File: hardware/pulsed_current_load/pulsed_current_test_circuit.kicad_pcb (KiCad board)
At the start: 2 copper layers, 50 x 50 mm, 19 parts, among them J1 Conn_02x03_Odd_Even, J2 Conn_02x03_Odd_Even, U1 eALD1116SAL, U2 eALD1116SAL, U3 eALD1116SAL

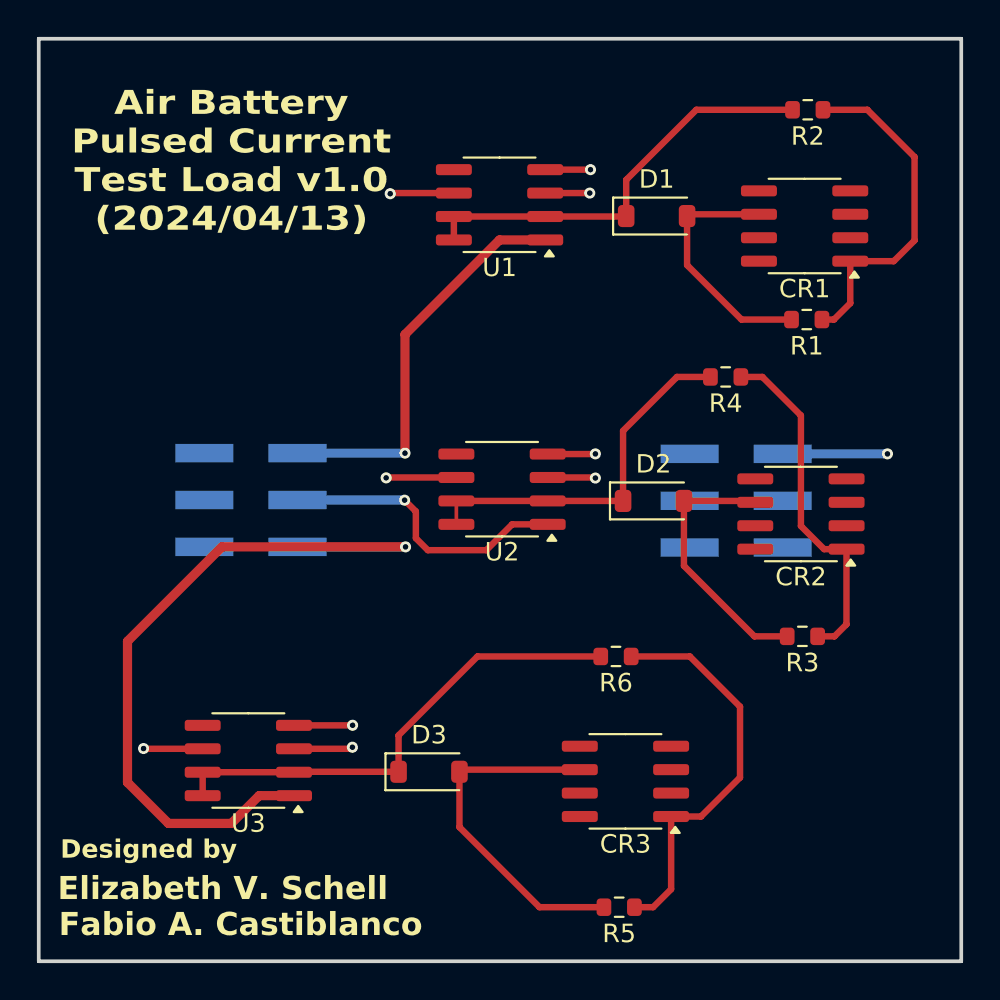
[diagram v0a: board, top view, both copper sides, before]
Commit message: added resistor load test board and adjustments to pulsed current load
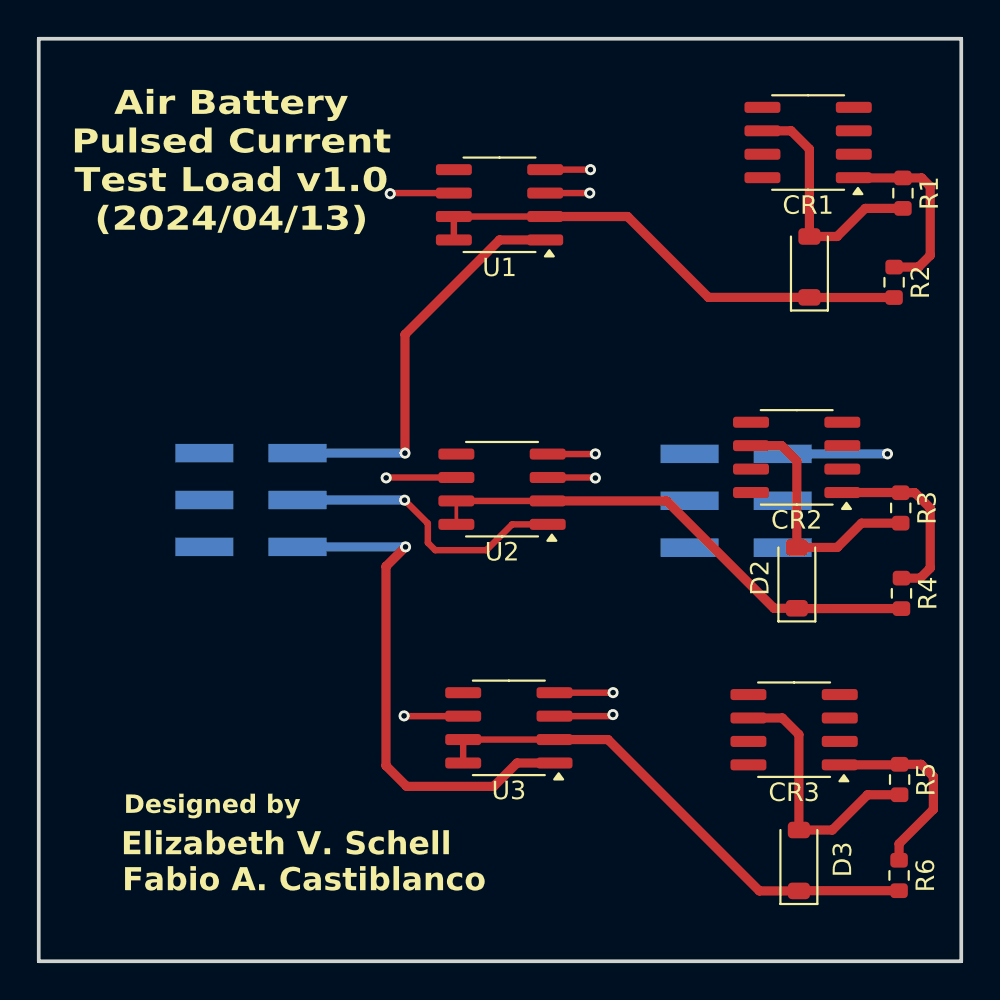
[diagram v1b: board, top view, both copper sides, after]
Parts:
- moved D3 20.6 mm to (184.2, 88.5), turned to 90 degrees
- moved R6 19.4 mm to (189.6, 89.3), turned to -90 degrees
- moved R5 16.7 mm to (189.7, 84.2), turned to -90 degrees
- moved R4 15.1 mm to (189.8, 74.1), turned to -90 degrees
- moved U3 14.2 mm to (168.5, 81.3)
- moved R2 10.5 mm to (189.4, 57.2), turned to -90 degrees
- moved CR3 9.56 mm to (183.9, 81.5)
- moved D2 8.82 mm to (184.1, 73.2), turned to 90 degrees
- moved R3 8.77 mm to (189.7, 69.4), turned to -90 degrees
- moved D1 8.73 mm to (184.8, 56.4), turned to 90 degrees
- moved R1 8.61 mm to (189.8, 52.4), turned to -90 degrees
- moved CR1 4.53 mm to (184.7, 49.6)
- moved CR2 3.08 mm to (184.1, 66.7)
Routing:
- net /P3+: track 40.0 -> 27.0 mm
- net Net-(CR3-ADJ): track 21.8 -> 10.7 mm
- net Net-(CR2-ADJ): track 19.0 -> 10.2 mm
- net Net-(CR1-ADJ): track 18.7 -> 10.3 mm
- net Net-(D2-K): track 20.0 -> 27.8 mm
- net Net-(CR3-V-): track 19.2 -> 14.5 mm
- net Net-(D1-K): track 23.6 -> 27.1 mm
- net Net-(D3-K): track 26.6 -> 28.3 mm
- net Net-(CR2-V-): track 14.6 -> 13.8 mm
